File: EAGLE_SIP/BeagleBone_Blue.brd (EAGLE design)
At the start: 86.4 x 54.6 mm, 268 parts, among them M1 JST_ZH_2, M2 JST_ZH_2, M3 JST_ZH_2, M4 JST_ZH_2, P10 SCHA5B0200, Q3 MOSFET-N, U1 TPD4S012_DRY_6, U4 TPD4S012_DRY_6, U5 24LC_32AT-I/OT, U6 SN74LVC1G07_DCK_5, U7 TPS2051B_D_8, U8 MTFC4GLDEA, Y1 CM200C-32.768KAZF-UT, Y2 445C33D24M00000

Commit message: Move pull-ups from VDD_3V3A to 3.3V
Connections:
- net 3.3V: now also R116.2, R120.2, R122.2, R140.2
- net VDD_3V3A: no longer R116.2, R118.2, R120.2, R122.2, R140.2
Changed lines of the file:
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@@
 <contactref element="C28" pad="1"/>
 <contactref element="R60" pad="2"/>
+<contactref element="R140" pad="2"/>
+<contactref element="R116" pad="2"/>
+<contactref element="R120" pad="2"/>
+<contactref element="R122" pad="2"/>
 <wire x1="111.7158" y1="-23.8633" x2="110.8014" y2="-11.4554" width="0" layer="19" extent="1-1"/>
 <wire x1="81.82" y1="-13.716" x2="110.8014" y2="-11.4554" width="0" layer="19" extent="1-1"/>
 <wire x1="77.751" y1="-14.265" x2="81.82" y2="-13.716" width="0" layer="19" extent="1-16"/>
 <wire x1="81.693" y1="-18.161" x2="81.82" y2="-13.716" width="0" layer="19" extent="1-1"/>
-<wire x1="82.1563" y1="-26.67" x2="81.693" y2="-18.161" width="0" layer="19" extent="1-1"/>
+<wire x1="78.1304" y1="-20.574" x2="81.693" y2="-18.161" width="0" layer="19" extent="1-16"/>
+<wire x1="82.1563" y1="-26.67" x2="78.1304" y2="-20.574" width="0" layer="19" extent="1-16"/>
 <wire x1="81.947" y1="-30.861" x2="82.1563" y2="-26.67" width="0" layer="19" extent="1-1"/>
 <wire x1="77.6875" y1="-31.537" x2="81.947" y2="-30.861" width="0" layer="19" extent="1-16"/>
+<wire x1="74.2696" y1="-30.0228" x2="77.6875" y2="-31.537" width="0" layer="19" extent="16-16"/>
 <wire x1="81.947" y1="-35.306" x2="81.947" y2="-30.861" width="0" layer="19" extent="1-1"/>
 <wire x1="73.0062" y1="-45.9994" x2="81.947" y2="-35.306" width="0" layer="19" extent="1-1"/>
 <wire x1="73.9046" y1="-53.1114" x2="73.0062" y2="-45.9994" width="0" layer="19" extent="1-1"/>
+<wire x1="64.4906" y1="-6.0833" x2="77.751" y2="-14.265" width="0" layer="19" extent="16-16"/>
+<wire x1="64.516" y1="-2.9718" x2="64.4906" y2="-6.0833" width="0" layer="19" extent="16-16"/>
 <wire x1="54.6989" y1="-49.3886" x2="73.0062" y2="-45.9994" width="0" layer="19" extent="1-16"/>
 <wire x1="52.5907" y1="-51.6001" x2="54.6989" y2="-49.3886" width="0" layer="19" extent="16-16"/>
@@
 <wire x1="40.6654" y1="-9.6012" x2="38.7985" y2="-9.4742" width="0" layer="19" extent="1-1"/>
 <wire x1="54.7751" y1="-26.6573" x2="50.1396" y2="-44.2976" width="0" layer="19" extent="1-1"/>
-<wire x1="54.8772" y1="18.0975" x2="40.6654" y2="-9.6012" width="0" layer="19" extent="1-1"/>
+<wire x1="54.8772" y1="18.0975" x2="64.516" y2="-2.9718" width="0" layer="19" extent="1-16"/>
 <wire x1="54.8772" y1="23.6093" x2="54.8772" y2="18.0975" width="0" layer="19" extent="1-1"/>
 </signal>
@@
 </signal>
 <signal name="VDD_3V3A">
-<contactref element="R140" pad="2"/>
-<contactref element="R116" pad="2"/>
-<contactref element="R118" pad="2"/>
-<contactref element="R120" pad="2"/>
-<contactref element="R122" pad="2"/>
 <contactref element="R157" pad="1"/>
 <contactref element="SIP" pad="E10"/>
@@
 <contactref element="SIP" pad="P13"/>
 <contactref element="SIP" pad="R15"/>
-<wire x1="64.4906" y1="-6.0833" x2="64.516" y2="-2.9718" width="0" layer="19" extent="16-16"/>
-<wire x1="78.1304" y1="-20.574" x2="64.4906" y2="-6.0833" width="0" layer="19" extent="16-16"/>
-<wire x1="74.2696" y1="-30.0228" x2="78.1304" y2="-20.574" width="0" layer="19" extent="16-16"/>
-<wire x1="74.2569" y1="-31.2928" x2="74.2696" y2="-30.0228" width="0" layer="19" extent="16-16"/>
-<wire x1="54.4195" y1="-31.115" x2="74.2569" y2="-31.2928" width="0" layer="19" extent="16-16"/>
-<wire x1="54.4195" y1="-32.385" x2="54.4195" y2="-31.115" width="0" layer="19" extent="16-16"/>
-<wire x1="53.1495" y1="-32.385" x2="54.4195" y2="-32.385" width="0" layer="19" extent="16-16"/>
-<wire x1="51.8795" y1="-32.385" x2="53.1495" y2="-32.385" width="0" layer="19" extent="16-16"/>
-<wire x1="50.6095" y1="-32.385" x2="51.8795" y2="-32.385" width="0" layer="19" extent="16-16"/>
-<wire x1="48.0695" y1="-32.385" x2="50.6095" y2="-32.385" width="0" layer="19" extent="16-16"/>
-<wire x1="46.7995" y1="-32.385" x2="48.0695" y2="-32.385" width="0" layer="19" extent="16-16"/>
-<wire x1="45.5295" y1="-32.385" x2="46.7995" y2="-32.385" width="0" layer="19" extent="16-16"/>
-<wire x1="44.2595" y1="-32.385" x2="45.5295" y2="-32.385" width="0" layer="19" extent="16-16"/>
-<wire x1="41.7195" y1="-31.115" x2="44.2595" y2="-32.385" width="0" layer="19" extent="16-16"/>
+<wire x1="46.7995" y1="-20.955" x2="48.0695" y2="-20.955" width="0" layer="19" extent="16-16"/>
+<wire x1="45.5295" y1="-20.955" x2="46.7995" y2="-20.955" width="0" layer="19" extent="16-16"/>
+<wire x1="44.2595" y1="-20.955" x2="45.5295" y2="-20.955" width="0" layer="19" extent="16-16"/>
+<wire x1="42.9895" y1="-22.225" x2="44.2595" y2="-20.955" width="0" layer="19" extent="16-16"/>
+<wire x1="42.9895" y1="-23.495" x2="42.9895" y2="-22.225" width="0" layer="19" extent="16-16"/>
+<wire x1="42.9895" y1="-24.765" x2="42.9895" y2="-23.495" width="0" layer="19" extent="16-16"/>
+<wire x1="42.9895" y1="-26.035" x2="42.9895" y2="-24.765" width="0" layer="19" extent="16-16"/>
+<wire x1="42.9895" y1="-27.305" x2="42.9895" y2="-26.035" width="0" layer="19" extent="16-16"/>
+<wire x1="42.9895" y1="-28.575" x2="42.9895" y2="-27.305" width="0" layer="19" extent="16-16"/>
+<wire x1="41.7195" y1="-31.115" x2="42.9895" y2="-28.575" width="0" layer="19" extent="16-16"/>
 <wire x1="41.7195" y1="-33.655" x2="41.7195" y2="-31.115" width="0" layer="19" extent="16-16"/>
-<wire x1="42.9895" y1="-28.575" x2="41.7195" y2="-31.115" width="0" layer="19" extent="16-16"/>
-<wire x1="42.9895" y1="-27.305" x2="42.9895" y2="-28.575" width="0" layer="19" extent="16-16"/>
-<wire x1="42.9895" y1="-26.035" x2="42.9895" y2="-27.305" width="0" layer="19" extent="16-16"/>
-<wire x1="42.9895" y1="-24.765" x2="42.9895" y2="-26.035" width="0" layer="19" extent="16-16"/>
-<wire x1="42.9895" y1="-23.495" x2="42.9895" y2="-24.765" width="0" layer="19" extent="16-16"/>
-<wire x1="42.9895" y1="-22.225" x2="42.9895" y2="-23.495" width="0" layer="19" extent="16-16"/>
-<wire x1="44.2595" y1="-20.955" x2="42.9895" y2="-22.225" width="0" layer="19" extent="16-16"/>
-<wire x1="45.5295" y1="-20.955" x2="44.2595" y2="-20.955" width="0" layer="19" extent="16-16"/>
-<wire x1="46.7995" y1="-20.955" x2="45.5295" y2="-20.955" width="0" layer="19" extent="16-16"/>
-<wire x1="48.0695" y1="-20.955" x2="46.7995" y2="-20.955" width="0" layer="19" extent="16-16"/>
+<wire x1="44.2595" y1="-32.385" x2="41.7195" y2="-31.115" width="0" layer="19" extent="16-16"/>
+<wire x1="45.5295" y1="-32.385" x2="44.2595" y2="-32.385" width="0" layer="19" extent="16-16"/>
+<wire x1="46.7995" y1="-32.385" x2="45.5295" y2="-32.385" width="0" layer="19" extent="16-16"/>
+<wire x1="48.0695" y1="-32.385" x2="46.7995" y2="-32.385" width="0" layer="19" extent="16-16"/>
+<wire x1="50.6095" y1="-32.385" x2="48.0695" y2="-32.385" width="0" layer="19" extent="16-16"/>
+<wire x1="51.8795" y1="-32.385" x2="50.6095" y2="-32.385" width="0" layer="19" extent="16-16"/>
+<wire x1="53.1495" y1="-32.385" x2="51.8795" y2="-32.385" width="0" layer="19" extent="16-16"/>
+<wire x1="54.4195" y1="-32.385" x2="53.1495" y2="-32.385" width="0" layer="19" extent="16-16"/>
+<wire x1="54.4195" y1="-31.115" x2="54.4195" y2="-32.385" width="0" layer="19" extent="16-16"/>
 <wire x1="15.875" y1="-19.5834" x2="42.9895" y2="-22.225" width="0" layer="19" extent="16-16"/>
 </signal>

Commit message: Move pull-ups from VDD_3V3A to 3.3V
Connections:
- net 3.3V: now also R118.2
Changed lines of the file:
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@@
 <contactref element="R120" pad="2"/>
 <contactref element="R122" pad="2"/>
+<contactref element="R118" pad="2"/>
 <wire x1="111.7158" y1="-23.8633" x2="110.8014" y2="-11.4554" width="0" layer="19" extent="1-1"/>
 <wire x1="81.82" y1="-13.716" x2="110.8014" y2="-11.4554" width="0" layer="19" extent="1-1"/>
@@
 <wire x1="81.947" y1="-30.861" x2="82.1563" y2="-26.67" width="0" layer="19" extent="1-1"/>
 <wire x1="77.6875" y1="-31.537" x2="81.947" y2="-30.861" width="0" layer="19" extent="1-16"/>
-<wire x1="74.2696" y1="-30.0228" x2="77.6875" y2="-31.537" width="0" layer="19" extent="16-16"/>
+<wire x1="74.2569" y1="-31.2928" x2="77.6875" y2="-31.537" width="0" layer="19" extent="16-16"/>
+<wire x1="74.2696" y1="-30.0228" x2="74.2569" y2="-31.2928" width="0" layer="19" extent="16-16"/>
 <wire x1="81.947" y1="-35.306" x2="81.947" y2="-30.861" width="0" layer="19" extent="1-1"/>
 <wire x1="73.0062" y1="-45.9994" x2="81.947" y2="-35.306" width="0" layer="19" extent="1-1"/>

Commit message: Move pull-ups from VDD_3V3A to 3.3V
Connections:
- net 3.3V: now also R157.1
- net VDD_3V3A: no longer R157.1
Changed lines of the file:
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@@
 <contactref element="R122" pad="2"/>
 <contactref element="R118" pad="2"/>
+<contactref element="R157" pad="1"/>
 <wire x1="111.7158" y1="-23.8633" x2="110.8014" y2="-11.4554" width="0" layer="19" extent="1-1"/>
 <wire x1="81.82" y1="-13.716" x2="110.8014" y2="-11.4554" width="0" layer="19" extent="1-1"/>
@@
 <wire x1="16.3322" y1="-21.971" x2="15.675" y2="-23.546" width="0" layer="19" extent="1-1"/>
 <wire x1="14.0462" y1="-21.971" x2="14.275" y2="-24.146" width="0" layer="19" extent="1-1"/>
+<wire x1="15.875" y1="-19.5834" x2="16.3322" y2="-21.971" width="0" layer="19" extent="1-16"/>
 <wire x1="12.1412" y1="-28.4988" x2="12.7" y2="-25.8572" width="0" layer="19" extent="1-1"/>
 <wire x1="21.6281" y1="-20.8026" x2="20.32" y2="-24.2062" width="0" layer="19" extent="1-1"/>
@@
 </signal>
 <signal name="VDD_3V3A">
-<contactref element="R157" pad="1"/>
 <contactref element="SIP" pad="E10"/>
 <contactref element="SIP" pad="E11"/>
@@
 <wire x1="54.4195" y1="-32.385" x2="53.1495" y2="-32.385" width="0" layer="19" extent="16-16"/>
 <wire x1="54.4195" y1="-31.115" x2="54.4195" y2="-32.385" width="0" layer="19" extent="16-16"/>
-<wire x1="15.875" y1="-19.5834" x2="42.9895" y2="-22.225" width="0" layer="19" extent="16-16"/>
 </signal>
 <signal name="VDD_3V3AUX">

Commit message: Remove unused VDD_3V3A
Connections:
- removed net VDD_3V3A: SIP.E10, SIP.E11, SIP.E12, SIP.E13, SIP.F14, SIP.G14, SIP.H14, SIP.J14, SIP.K14, SIP.L14, SIP.N15, SIP.N5, SIP.P10, SIP.P11, SIP.P12, SIP.P13, SIP.P5, SIP.P6, SIP.P7, SIP.P8, SIP.R15
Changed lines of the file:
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@@
 <wire x1="18.923" y1="-23.0632" x2="36.6395" y2="-18.415" width="0" layer="19" extent="1-16"/>
-</signal>
-<signal name="VDD_3V3A">
-<contactref element="SIP" pad="E10"/>
-<contactref element="SIP" pad="E11"/>
-<contactref element="SIP" pad="E12"/>
-<contactref element="SIP" pad="E13"/>
-<contactref element="SIP" pad="F14"/>
-<contactref element="SIP" pad="G14"/>
-<contactref element="SIP" pad="H14"/>
-<contactref element="SIP" pad="J14"/>
-<contactref element="SIP" pad="K14"/>
-<contactref element="SIP" pad="L14"/>
-<contactref element="SIP" pad="N5"/>
-<contactref element="SIP" pad="N15"/>
-<contactref element="SIP" pad="P5"/>
-<contactref element="SIP" pad="P6"/>
-<contactref element="SIP" pad="P7"/>
-<contactref element="SIP" pad="P8"/>
-<contactref element="SIP" pad="P10"/>
-<contactref element="SIP" pad="P11"/>
-<contactref element="SIP" pad="P12"/>
-<contactref element="SIP" pad="P13"/>
-<contactref element="SIP" pad="R15"/>
-<wire x1="46.7995" y1="-20.955" x2="48.0695" y2="-20.955" width="0" layer="19" extent="16-16"/>
-<wire x1="45.5295" y1="-20.955" x2="46.7995" y2="-20.955" width="0" layer="19" extent="16-16"/>
-<wire x1="44.2595" y1="-20.955" x2="45.5295" y2="-20.955" width="0" layer="19" extent="16-16"/>
-<wire x1="42.9895" y1="-22.225" x2="44.2595" y2="-20.955" width="0" layer="19" extent="16-16"/>
-<wire x1="42.9895" y1="-23.495" x2="42.9895" y2="-22.225" width="0" layer="19" extent="16-16"/>
-<wire x1="42.9895" y1="-24.765" x2="42.9895" y2="-23.495" width="0" layer="19" extent="16-16"/>
-<wire x1="42.9895" y1="-26.035" x2="42.9895" y2="-24.765" width="0" layer="19" extent="16-16"/>
-<wire x1="42.9895" y1="-27.305" x2="42.9895" y2="-26.035" width="0" layer="19" extent="16-16"/>
-<wire x1="42.9895" y1="-28.575" x2="42.9895" y2="-27.305" width="0" layer="19" extent="16-16"/>
-<wire x1="41.7195" y1="-31.115" x2="42.9895" y2="-28.575" width="0" layer="19" extent="16-16"/>
-<wire x1="41.7195" y1="-33.655" x2="41.7195" y2="-31.115" width="0" layer="19" extent="16-16"/>
-<wire x1="44.2595" y1="-32.385" x2="41.7195" y2="-31.115" width="0" layer="19" extent="16-16"/>
-<wire x1="45.5295" y1="-32.385" x2="44.2595" y2="-32.385" width="0" layer="19" extent="16-16"/>
-<wire x1="46.7995" y1="-32.385" x2="45.5295" y2="-32.385" width="0" layer="19" extent="16-16"/>
-<wire x1="48.0695" y1="-32.385" x2="46.7995" y2="-32.385" width="0" layer="19" extent="16-16"/>
-<wire x1="50.6095" y1="-32.385" x2="48.0695" y2="-32.385" width="0" layer="19" extent="16-16"/>
-<wire x1="51.8795" y1="-32.385" x2="50.6095" y2="-32.385" width="0" layer="19" extent="16-16"/>
-<wire x1="53.1495" y1="-32.385" x2="51.8795" y2="-32.385" width="0" layer="19" extent="16-16"/>
-<wire x1="54.4195" y1="-32.385" x2="53.1495" y2="-32.385" width="0" layer="19" extent="16-16"/>
-<wire x1="54.4195" y1="-31.115" x2="54.4195" y2="-32.385" width="0" layer="19" extent="16-16"/>
 </signal>
 <signal name="VDD_3V3AUX">

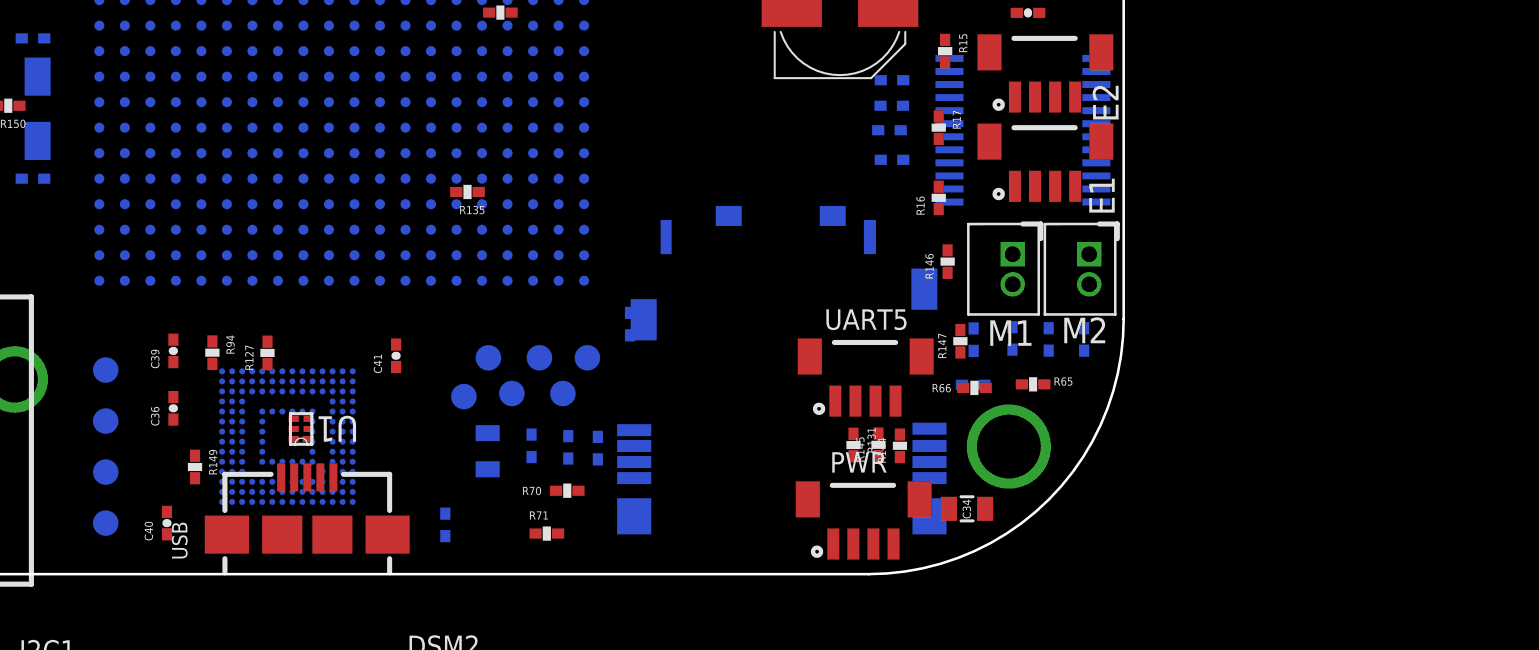
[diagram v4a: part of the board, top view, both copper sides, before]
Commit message: Look at moving eMMC and test points
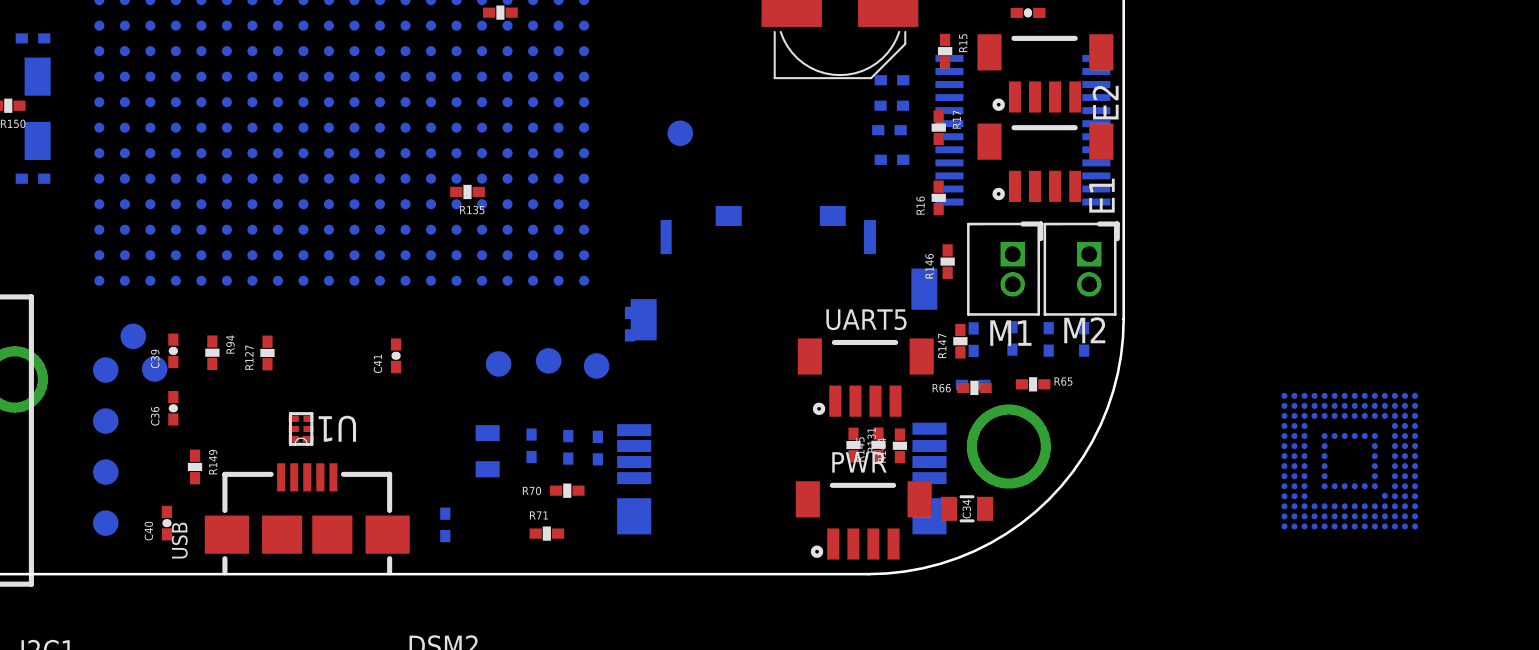
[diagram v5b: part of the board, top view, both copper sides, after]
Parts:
- moved U8 52.9 mm to (97.6, -49.0)
- moved TP6 17.7 mm to (37.1, -42.8)
- moved TP7 15.5 mm to (38.1, -44.4)
- moved TP4 15.4 mm to (64.3, -32.7)
- moved TP1 4.43 mm to (55.2, -44.1)
- moved TP3 2.17 mm to (60.1, -44.2)
- moved TP2 0.48 mm to (57.7, -44.0)

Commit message: Delete some test points I know I will not use
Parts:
- removed TP10, TP3, TP4, TP6, TP8: TPSQB1,27, testpad:B1,27
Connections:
- removed net N$13: SIP.Y14, TP6.TP
- removed net N$20: SIP.Y17, TP8.TP
- removed net N$22: SIP.Y20, TP10.TP
- removed net N$7: SIP.Y1, TP3.TP
- removed net N$9: SIP.W1, TP4.TP
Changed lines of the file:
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@@
 <attribute name="TP_SIGNAL_NAME" value="" x="55.245" y="-44.1452" size="1.778" layer="28" rot="MR0" display="off"/>
-</element>
-<element name="TP10" library="testpad" package="B1,27" value="TPSQB1,27" x="35.687" y="-49.53" rot="MR0">
-<attribute name="TP_SIGNAL_NAME" value="" x="35.687" y="-49.53" size="1.778" layer="28" rot="MR0" display="off"/>
 </element>
 <element name="TP11" library="testpad" package="B1,27" value="TPSQB1,27" x="35.687" y="-52.07" rot="MR0">
@@
 <attribute name="TP_SIGNAL_NAME" value="" x="48.1203" y="-17.6784" size="1.778" layer="27" display="off"/>
 </element>
-<element name="TP3" library="testpad" package="B1,27" value="TPSQB1,27" x="60.1218" y="-44.2468" rot="MR0">
-<attribute name="TP_SIGNAL_NAME" value="" x="60.1218" y="-44.2468" size="1.778" layer="28" rot="MR0" display="off"/>
-</element>
-<element name="TP4" library="testpad" package="B1,27" value="TPSQB1,27" x="64.2874" y="-32.6644" rot="MR0">
-<attribute name="TP_SIGNAL_NAME" value="" x="64.2874" y="-32.6644" size="1.778" layer="28" rot="MR0" display="off"/>
-</element>
 <element name="TP5" library="testpad" package="B1,27" value="TPSQB1,27" x="51.7017" y="-19.5072">
 <attribute name="TP_SIGNAL_NAME" value="" x="51.7017" y="-19.5072" size="1.778" layer="27" display="off"/>
 </element>
-<element name="TP6" library="testpad" package="B1,27" value="TPSQB1,27" x="37.0586" y="-42.7736" rot="MR0">
-<attribute name="TP_SIGNAL_NAME" value="" x="37.0586" y="-42.7736" size="1.778" layer="28" rot="MR0" display="off"/>
-</element>
 <element name="TP7" library="testpad" package="B1,27" value="TPSQB1,27" x="38.1254" y="-44.3992" rot="MR0">
 <attribute name="TP_SIGNAL_NAME" value="" x="38.1254" y="-44.3992" size="1.778" layer="28" rot="MR0" display="off"/>
-</element>
-<element name="TP8" library="testpad" package="B1,27" value="TPSQB1,27" x="35.687" y="-44.45" rot="MR0">
-<attribute name="TP_SIGNAL_NAME" value="" x="35.687" y="-44.45" size="1.778" layer="28" rot="MR0" display="off"/>
 </element>
 <element name="TP9" library="testpad" package="B1,27" value="TPSQB1,27" x="35.687" y="-46.99" rot="MR0">
@@
 <wire x1="57.7342" y1="-43.9928" x2="56.9595" y2="-40.005" width="0" layer="19" extent="16-16"/>
 </signal>
-<signal name="N$7">
-<contactref element="SIP" pad="Y1"/>
-<contactref element="TP3" pad="TP"/>
-<wire x1="60.1218" y1="-44.2468" x2="59.4995" y2="-40.005" width="0" layer="19" extent="16-16"/>
-</signal>
-<signal name="N$9">
-<contactref element="SIP" pad="W1"/>
-<contactref element="TP4" pad="TP"/>
-<wire x1="64.2874" y1="-32.6644" x2="59.4995" y2="-38.735" width="0" layer="19" extent="16-16"/>
-</signal>
 <signal name="N$12">
 <contactref element="SIP" pad="D19"/>
@@
 <wire x1="37.9095" y1="-17.145" x2="36.6395" y2="-17.145" width="0" layer="19" extent="16-16"/>
 </signal>
-<signal name="N$13">
-<contactref element="SIP" pad="Y14"/>
-<contactref element="TP6" pad="TP"/>
-<wire x1="42.9895" y1="-40.005" x2="37.0586" y2="-42.7736" width="0" layer="19" extent="16-16"/>
-</signal>
 <signal name="N$19">
 <contactref element="SIP" pad="Y13"/>
@@
 <wire x1="44.2595" y1="-40.005" x2="38.1254" y2="-44.3992" width="0" layer="19" extent="16-16"/>
 </signal>
-<signal name="N$20">
-<contactref element="SIP" pad="Y17"/>
-<contactref element="TP8" pad="TP"/>
-<wire x1="39.1795" y1="-40.005" x2="35.687" y2="-44.45" width="0" layer="19" extent="16-16"/>
-</signal>
 <signal name="N$21">
 <contactref element="SIP" pad="Y16"/>
@@
 <wire x1="40.4495" y1="-40.005" x2="35.687" y2="-46.99" width="0" layer="19" extent="16-16"/>
 </signal>
-<signal name="N$22">
-<contactref element="SIP" pad="Y20"/>
-<contactref element="TP10" pad="TP"/>
-<wire x1="35.3695" y1="-40.005" x2="35.687" y2="-49.53" width="0" layer="19" extent="16-16"/>
-</signal>
 <signal name="N$23">

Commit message: Delete extraneous VDD_RTC connections and save shortest route
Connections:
- net VDD_RTC: no longer SIP.D7, SIP.E6, SIP.F9, SIP.K13, SIP.N6, SIP.P14, SIP.P9
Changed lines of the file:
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@@
 <signal name="VDD_RTC">
 <contactref element="U6" pad="5"/>
-<contactref element="SIP" pad="D7"/>
-<contactref element="SIP" pad="E6"/>
 <contactref element="SIP" pad="E14"/>
-<contactref element="SIP" pad="F9"/>
-<contactref element="SIP" pad="K13"/>
-<contactref element="SIP" pad="N6"/>
-<contactref element="SIP" pad="P9"/>
-<contactref element="SIP" pad="P14"/>
-<wire x1="53.1495" y1="-20.955" x2="51.8795" y2="-19.685" width="0" layer="19" extent="16-16"/>
-<wire x1="49.3395" y1="-22.225" x2="51.8795" y2="-19.685" width="0" layer="19" extent="16-16"/>
-<wire x1="42.9895" y1="-20.955" x2="49.3395" y2="-22.225" width="0" layer="19" extent="16-16"/>
-<wire x1="44.2595" y1="-27.305" x2="42.9895" y2="-20.955" width="0" layer="19" extent="16-16"/>
-<wire x1="42.9895" y1="-32.385" x2="44.2595" y2="-27.305" width="0" layer="19" extent="16-16"/>
-<wire x1="49.3395" y1="-32.385" x2="42.9895" y2="-32.385" width="0" layer="19" extent="16-16"/>
-<wire x1="53.1495" y1="-31.115" x2="49.3395" y2="-32.385" width="0" layer="19" extent="16-16"/>
 <wire x1="23.1924875" y1="-18.6182" x2="42.9895" y2="-20.955" width="0" layer="19" extent="1-16"/>
 </signal>
